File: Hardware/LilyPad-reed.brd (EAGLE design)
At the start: 7.6 x 33.4 mm, 7 parts

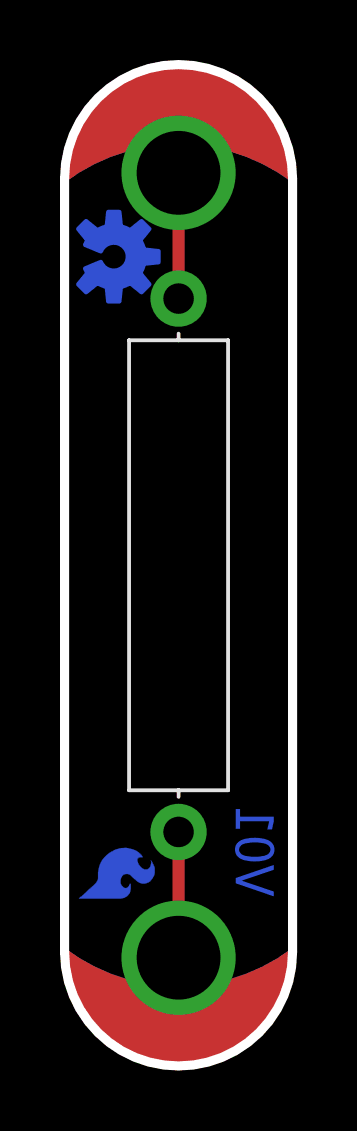
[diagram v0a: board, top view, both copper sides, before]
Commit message: QC checklist changes
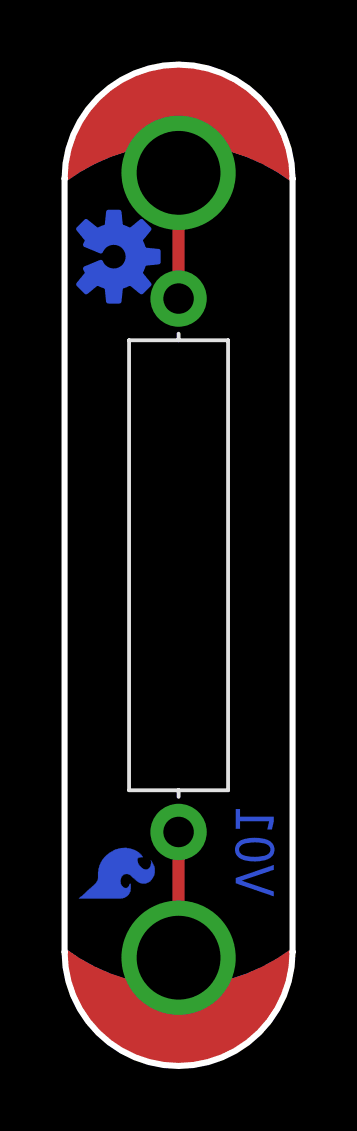
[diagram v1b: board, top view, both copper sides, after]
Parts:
- S1: value SWITCH-MOMENTARY-2PTH_REED2 -> REED
- moved FRAME1 77.3 mm to (-24.4, -38.1)
- renumbered REED to S1
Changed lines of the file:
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@@
 <board>
 <plain>
-<wire x1="-3.8" y1="12.89" x2="3.8" y2="12.89" width="0.3048" layer="20" curve="-180"/>
-<wire x1="3.8" y1="-12.89" x2="-3.8" y2="-12.89" width="0.3048" layer="20" curve="-180"/>
-<wire x1="-3.8" y1="12.89" x2="-3.8" y2="-12.89" width="0.3048" layer="20"/>
-<wire x1="3.8" y1="12.89" x2="3.8" y2="-12.89" width="0.3048" layer="20"/>
-<text x="-60.96" y="0" size="1.778" layer="51" font="vector" ratio="15">Dia Campbell</text>
+<wire x1="-3.8" y1="12.89" x2="3.8" y2="12.89" width="0.2032" layer="20" curve="-180"/>
+<wire x1="3.8" y1="-12.89" x2="-3.8" y2="-12.89" width="0.2032" layer="20" curve="-180"/>
+<wire x1="-3.8" y1="12.89" x2="-3.8" y2="-12.89" width="0.2032" layer="20"/>
+<wire x1="3.8" y1="12.89" x2="3.8" y2="-12.89" width="0.2032" layer="20"/>
+<text x="7.62" y="-38.1" size="1.778" layer="51" font="vector" ratio="15">Dia Campbell</text>
 <text x="1.905" y="-11.049" size="1.27" layer="16" font="vector" ratio="15" rot="MR90">V01</text>
 <text x="6.35" y="22.86" size="1.778" layer="52" font="vector" ratio="15">purple 0.08mm</text>
 <text x="-10.16" y="21.59" size="1.778" layer="51" font="vector" ratio="15">purple 0.8mm</text>
-<dimension x1="-3.8" y1="12.89" x2="3.81" y2="11.43" x3="0.005" y3="-21.59" textsize="1.778" textratio="15" layer="51" dtype="horizontal" unit="inch"/>
-<dimension x1="0" y1="16.637" x2="0.127" y2="-16.637" x3="11.43" y3="0" textsize="1.778" textratio="15" layer="51" dtype="vertical" unit="inch"/>
-<text x="-13.97" y="-26.67" size="1.778" layer="51" font="vector" ratio="15">Dimensions in inches</text>
+<dimension x1="-3.8" y1="12.89" x2="3.81" y2="11.43" x3="0.005" y3="-21.59" textsize="1.778" textratio="15" layer="47" dtype="horizontal" unit="inch"/>
+<dimension x1="0" y1="16.637" x2="0.127" y2="-16.637" x3="11.43" y3="0" textsize="1.778" textratio="15" layer="47" dtype="vertical" unit="inch"/>
+<text x="-13.97" y="-26.67" size="1.778" layer="47" font="vector" ratio="15">Dimensions in inches</text>
 </plain>
 <attributes>
@@
 <element name="SLIDEOFF" library="LilyPad-Wearables" package="PETAL-MEDIUM-2SIDE" value="SEWTAP8" x="0" y="-12.827"/>
 <element name="SLIDEON" library="LilyPad-Wearables" package="PETAL-MEDIUM-2SIDE" value="SEWTAP8" x="0" y="12.827" rot="R180"/>
-<element name="REED" library="SparkFun-Electromechanical" package="REED_SWITCH_PLASTIC" value="SWITCH-MOMENTARY-2PTH_REED2" x="0" y="0" rot="R270">
+<element name="S1" library="SparkFun-Electromechanical" package="REED_SWITCH_PLASTIC" value="REED" x="0" y="0" rot="R270">
 <attribute name="PROD_ID" value="SWCH-10467" x="0" y="0" size="1.778" layer="27" rot="R270" display="off"/>
 </element>
 <element name="U$1" library="LilyPad-Wearables" package="LOGO-LILYPAD" value="LOGO-LPLP" x="0.127" y="-0.127" rot="MR90"/>
-<element name="FRAME1" library="SparkFun-Aesthetics" package="CREATIVE_COMMONS" value="" x="-91.73185625" y="0">
-<attribute name="VERSION" value="v01" x="-91.73185625" y="0" size="1.778" layer="27" display="off"/>
-<attribute name="DESIGNER" value="NAME" x="-91.73185625" y="0" size="1.778" layer="27" display="off"/>
+<element name="FRAME1" library="SparkFun-Aesthetics" package="CREATIVE_COMMONS" value="" x="-24.42185625" y="-38.1">
+<attribute name="VERSION" value="v01" x="-24.42185625" y="-38.1" size="1.778" layer="27" display="off"/>
+<attribute name="DESIGNER" value="NAME" x="-24.42185625" y="-38.1" size="1.778" layer="27" display="off"/>
 </element>
 <element name="LOGO1" library="SparkFun-Aesthetics" package="OSHW-LOGO-S_COPPER" value="OSHW-LOGOS-COPPER" x="-2.159" y="10.287" rot="MR90"/>
@@
 <signal name="N$1">
 <contactref element="SLIDEOFF" pad="1"/>
-<contactref element="REED" pad="P$2"/>
+<contactref element="S1" pad="P$2"/>
 <wire x1="0" y1="-13.081" x2="0" y2="-8.89" width="0.4064" layer="1"/>
 </signal>
 <signal name="N$2">
-<contactref element="REED" pad="P$1"/>
+<contactref element="S1" pad="P$1"/>
 <contactref element="SLIDEON" pad="1"/>
 <wire x1="0" y1="13.081" x2="0" y2="8.89" width="0.4064" layer="1"/>

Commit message: Fixed version number for redboards
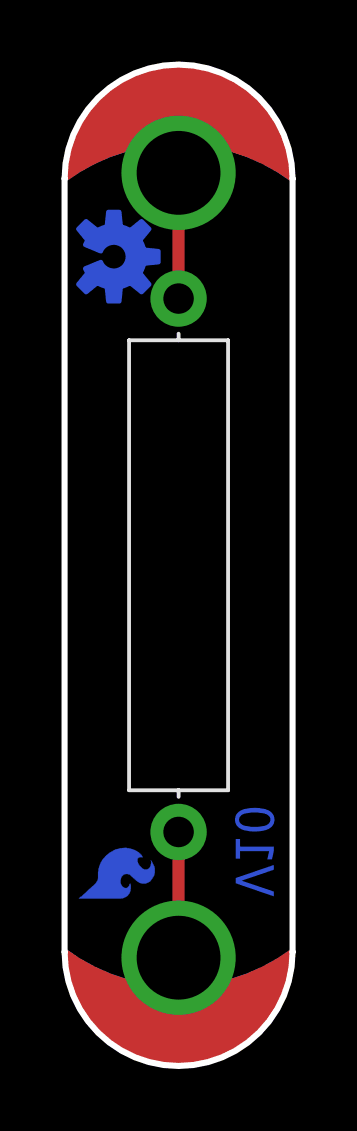
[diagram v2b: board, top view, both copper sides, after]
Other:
- board text added: "V10"
- board text removed: "V01"
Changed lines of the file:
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@@
 <wire x1="3.8" y1="12.89" x2="3.8" y2="-12.89" width="0.2032" layer="20"/>
 <text x="7.62" y="-38.1" size="1.778" layer="51" font="vector" ratio="15">Dia Campbell</text>
-<text x="1.905" y="-11.049" size="1.27" layer="16" font="vector" ratio="15" rot="MR90">V01</text>
+<text x="1.905" y="-11.049" size="1.27" layer="16" font="vector" ratio="15" rot="MR90">V10</text>
 <text x="6.35" y="22.86" size="1.778" layer="52" font="vector" ratio="15">purple 0.08mm</text>
 <text x="-10.16" y="21.59" size="1.778" layer="51" font="vector" ratio="15">purple 0.8mm</text>
